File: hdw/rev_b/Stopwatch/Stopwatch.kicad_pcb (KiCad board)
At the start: 4 copper layers, 80 x 45 mm, 194 parts, among them J201 +12V IN, Q301 BSS214NW, Q302 ZXMS6004FFTA, SW601 Cap_Touch, SW602 Cap_Touch, SW603 Cap_Touch, U1001 4026, U1002 HDSP-7503, U1101 4026, U1102 HDSP-7503, U1201 4026, U1202 HDSP-7503, U1301 74LVC1G97, U1302 74LVC1G97, U1303 74LVC1G97, U1304 74LVC1G97, U1305 74LVC1G97, U1306 74LVC1G97, U1307 74LVC1G97, U1401 74LVC1G97, U1402 74LVC1G97, U1403 74LVC1G97, U1404 74LVC1G97, U1405 74LVC1G97, U1406 74LVC1G97, U1407 74LVC1G97, U201 TPS26600RHFT, U301 TPS62130A, U401 74LVC1G97, U402 CD4024, U403 CD4040, U501 74LVC1G97, U502 74LVC1G97, U503 74LVC1G97, U504 74LVC1G97, U505 74LVC1G97, U601 AT42QT1010-TSHR, U602 AT42QT1010-TSHR, U603 AT42QT1010-TSHR, U604 74LVC1G97, U605 74LVC1G97, U606 74LVC1G97, U607 74LVC1G80, U608 74LVC1G80, U701 4026, U702 HDSP-7503, U801 4026, U802 HDSP-7503, U901 4026, U902 HDSP-7503, X401 ECS-327KE

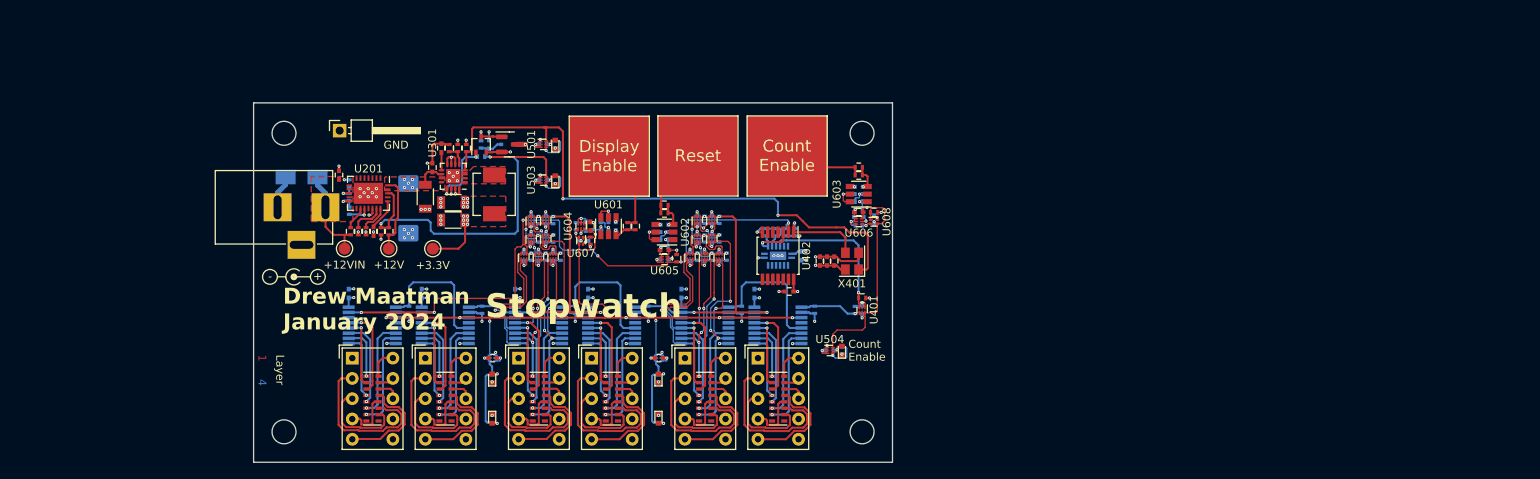
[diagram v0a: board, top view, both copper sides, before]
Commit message: converted pcb to rev b
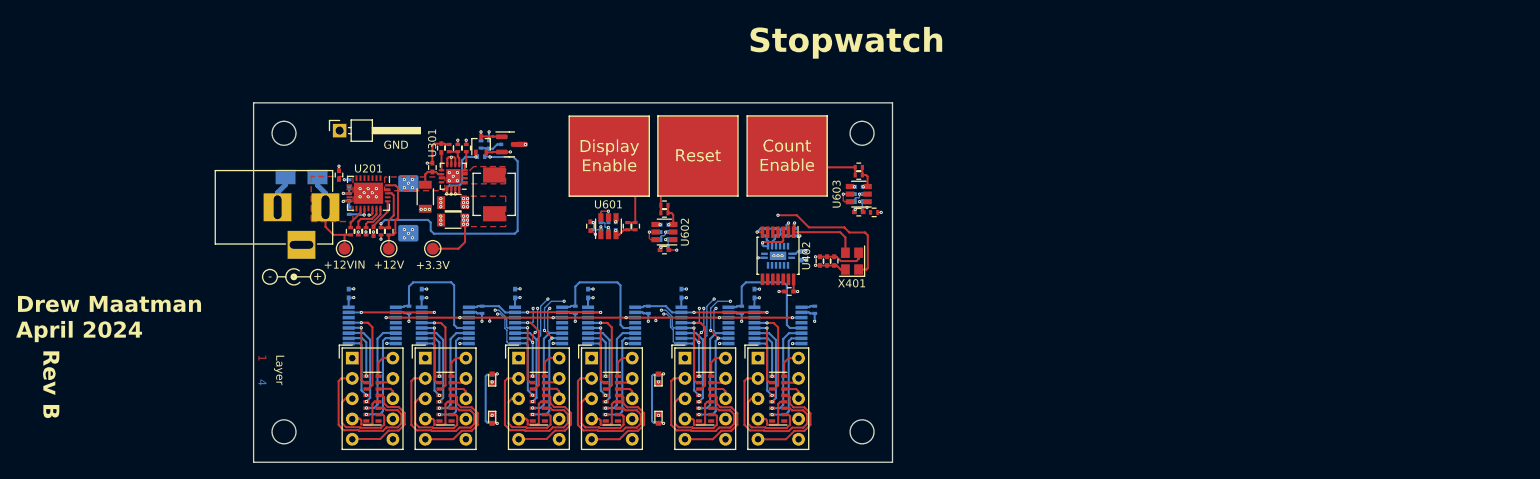
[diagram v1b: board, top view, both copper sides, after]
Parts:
- removed C1301, C1302, C1303, C1304, C1305, C1306, C1307, C1401, C1402, C1403, C1404, C1405, C1406, C1407, C405, C501, C502, C503, C504, C505, C610, C611, C612, C613, C614: 0.1uF, Capacitors_SMD:C_0402
- removed D501, D504, D505: Green, LEDs:LED_0402
- removed R1301, R1302, R1303, R1304, R1305, R1306, R1307, R1401, R1402, R1403, R1404, R1405, R1406, R1407, R402, R404, R613, R614, R615, R616: 10k, Resistors_SMD:R_0402
- removed R501, R504, R505: 1k, Resistors_SMD:R_0402
- removed U1301, U1302, U1303, U1304, U1305, U1306, U1307, U1401, U1402, U1403, U1404, U1405, U1406, U1407, U401, U501, U502, U503, U504, U505, U604, U605, U606: 74LVC1G97, Package_SON:Fairchild_MicroPak2-6_1.0x1.0mm_P0.35mm
- removed U607, U608: 74LVC1G80, Package_SON:Texas_X2SON-5_0.8x0.8mm_P0.48mm
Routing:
- net GND: track 144.6 -> 72.7 mm, vias 88 -> 61
- net Count_Reset: track 87.7 -> 17.9 mm, vias 8 -> 3
- net POS3P3_PGOOD: track 74.4 -> 20.0 mm, vias 2 -> 1
- net +3.3V: track 79.3 -> 43.8 mm, vias 62 -> 32
- net Count_Enable: track 26.2 -> 0.00 mm
- net Display_Enable: track 84.3 -> 58.6 mm
- net 1Hz_Clock_SRC: track 18.5 -> 0.00 mm, vias 1 -> 0
- net Seconds_Reset: track 32.9 -> 18.5 mm, vias 3 -> 2
- net Minutes_Reset: track 32.9 -> 18.5 mm, vias 3 -> 2
- net Stage04_SEG_B: track 23.5 -> 12.9 mm
- net Stage02_SEG_B: track 23.6 -> 13.0 mm
- net Stage04_SEG_D: track 23.4 -> 13.5 mm
- net Stage02_SEG_D: track 23.3 -> 13.5 mm
- net POS12_PGOOD: track 47.8 -> 38.5 mm
- net Stage04_SEG_G: track 29.0 -> 19.8 mm
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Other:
- board text added: "Drew Maatman April 2024"
- board text added: "Rev B"
- board text added: "Stopwatch Rev B Pads: 783 Vias: 309 Track Segments: 1922 Nets: 219 Components: 192"
- board text removed: "Drew Maatman January 2024"
- board text removed: "Stopwatch Rev A Pads: 783 Vias: 309 Track Segments: 1922 Nets: 219 Components: 192"

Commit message: integrated SC70 gates
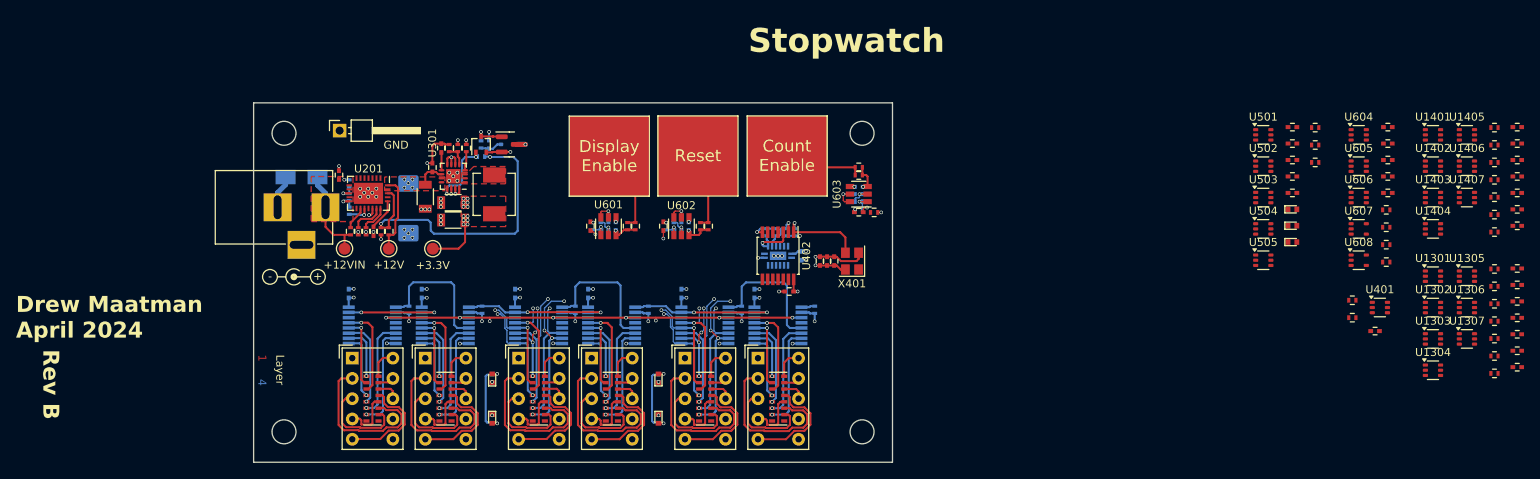
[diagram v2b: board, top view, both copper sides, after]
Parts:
- added C1301: 0.1uF, Capacitors_SMD:C_0402, F.Cu at (243.7, 102.0)
- added C1302: 0.1uF, Capacitors_SMD:C_0402, F.Cu at (243.7, 104.0)
- added C1303: 0.1uF, Capacitors_SMD:C_0402, F.Cu at (243.7, 106.1)
- added C1304: 0.1uF, Capacitors_SMD:C_0402, F.Cu at (243.7, 108.1)
- added C1305: 0.1uF, Capacitors_SMD:C_0402, F.Cu at (243.7, 110.2)
- added C1306: 0.1uF, Capacitors_SMD:C_0402, F.Cu at (243.7, 112.3)
- added C1307: 0.1uF, Capacitors_SMD:C_0402, F.Cu at (243.7, 114.3)
- added C1401: 0.1uF, Capacitors_SMD:C_0402, F.Cu at (243.7, 84.3)
- added C1402: 0.1uF, Capacitors_SMD:C_0402, F.Cu at (243.7, 86.3)
- added C1403: 0.1uF, Capacitors_SMD:C_0402, F.Cu at (243.7, 88.4)
- added C1404: 0.1uF, Capacitors_SMD:C_0402, F.Cu at (243.7, 90.4)
- added C1405: 0.1uF, Capacitors_SMD:C_0402, F.Cu at (243.7, 92.5)
- added C1406: 0.1uF, Capacitors_SMD:C_0402, F.Cu at (243.7, 94.6)
- added C1407: 0.1uF, Capacitors_SMD:C_0402, F.Cu at (243.7, 96.6)
- added C405: 0.1uF, Capacitors_SMD:C_0402, F.Cu at (225.9, 109.8)
- added C501: 0.1uF, Capacitors_SMD:C_0402, F.Cu at (215.6, 84.3)
- added C502: 0.1uF, Capacitors_SMD:C_0402, F.Cu at (215.6, 86.3)
- added C503: 0.1uF, Capacitors_SMD:C_0402, F.Cu at (215.6, 88.4)
- added C504: 0.1uF, Capacitors_SMD:C_0402, F.Cu at (215.6, 90.4)
- added C505: 0.1uF, Capacitors_SMD:C_0402, F.Cu at (215.6, 92.5)
- added C610: 0.1uF, Capacitors_SMD:C_0402, F.Cu at (227.5, 84.3)
- added C611: 0.1uF, Capacitors_SMD:C_0402, F.Cu at (227.5, 86.3)
- added C612: 0.1uF, Capacitors_SMD:C_0402, F.Cu at (227.5, 88.4)
- added C613: 0.1uF, Capacitors_SMD:C_0402, F.Cu at (227.5, 90.4)
- added C614: 0.1uF, Capacitors_SMD:C_0402, F.Cu at (227.5, 92.5)
- added D501: Green, LEDs:LED_0402, F.Cu at (215.6, 94.6)
- added D504: Green, LEDs:LED_0402, F.Cu at (215.6, 96.6)
- added D505: Green, LEDs:LED_0402, F.Cu at (215.6, 98.7)
- added R1301: 10k, Resistors_SMD:R_0402, F.Cu at (240.9, 102.0)
- added R1302: 10k, Resistors_SMD:R_0402, F.Cu at (240.9, 104.2)
- added R1303: 10k, Resistors_SMD:R_0402, F.Cu at (240.9, 106.4)
- added R1304: 10k, Resistors_SMD:R_0402, F.Cu at (240.9, 108.6)
- added R1305: 10k, Resistors_SMD:R_0402, F.Cu at (240.9, 110.7)
- added R1306: 10k, Resistors_SMD:R_0402, F.Cu at (240.9, 112.9)
- added R1307: 10k, Resistors_SMD:R_0402, F.Cu at (240.9, 115.1)
- added R1401: 10k, Resistors_SMD:R_0402, F.Cu at (240.9, 84.3)
- added R1402: 10k, Resistors_SMD:R_0402, F.Cu at (240.9, 86.5)
- added R1403: 10k, Resistors_SMD:R_0402, F.Cu at (240.9, 88.7)
- added R1404: 10k, Resistors_SMD:R_0402, F.Cu at (240.9, 90.9)
- added R1405: 10k, Resistors_SMD:R_0402, F.Cu at (240.9, 93.0)
- added R1406: 10k, Resistors_SMD:R_0402, F.Cu at (240.9, 95.2)
- added R1407: 10k, Resistors_SMD:R_0402, F.Cu at (240.9, 97.4)
- added R402: 10k, Resistors_SMD:R_0402, F.Cu at (223.1, 105.9)
- added R404: 10k, Resistors_SMD:R_0402, F.Cu at (223.1, 108.1)
- added R501: 1k, Resistors_SMD:R_0402, F.Cu at (218.4, 84.3)
- added R504: 1k, Resistors_SMD:R_0402, F.Cu at (218.4, 86.5)
- added R505: 1k, Resistors_SMD:R_0402, F.Cu at (218.4, 88.7)
- added R613: 10k, Resistors_SMD:R_0402, F.Cu at (227.3, 94.6)
- added R614: 10k, Resistors_SMD:R_0402, F.Cu at (227.3, 96.8)
- added R615: 10k, Resistors_SMD:R_0402, F.Cu at (227.3, 99.0)
- added R616: 10k, Resistors_SMD:R_0402, F.Cu at (227.3, 101.2)
- added U1301: 74LVC1G97, Package_TO_SOT_SMD:SOT-363_SC-70-6, F.Cu at (233.2, 102.9)
- added U1302: 74LVC1G97, Package_TO_SOT_SMD:SOT-363_SC-70-6, F.Cu at (233.2, 106.9)
- added U1303: 74LVC1G97, Package_TO_SOT_SMD:SOT-363_SC-70-6, F.Cu at (233.2, 110.8)
- added U1304: 74LVC1G97, Package_TO_SOT_SMD:SOT-363_SC-70-6, F.Cu at (233.2, 114.7)
- added U1305: 74LVC1G97, Package_TO_SOT_SMD:SOT-363_SC-70-6, F.Cu at (237.4, 102.9)
- added U1306: 74LVC1G97, Package_TO_SOT_SMD:SOT-363_SC-70-6, F.Cu at (237.4, 106.9)
- added U1307: 74LVC1G97, Package_TO_SOT_SMD:SOT-363_SC-70-6, F.Cu at (237.4, 110.8)
- added U1401: 74LVC1G97, Package_TO_SOT_SMD:SOT-363_SC-70-6, F.Cu at (233.2, 85.2)
- added U1402: 74LVC1G97, Package_TO_SOT_SMD:SOT-363_SC-70-6, F.Cu at (233.2, 89.2)
- added U1403: 74LVC1G97, Package_TO_SOT_SMD:SOT-363_SC-70-6, F.Cu at (233.2, 93.1)
- added U1404: 74LVC1G97, Package_TO_SOT_SMD:SOT-363_SC-70-6, F.Cu at (233.2, 97.0)
- added U1405: 74LVC1G97, Package_TO_SOT_SMD:SOT-363_SC-70-6, F.Cu at (237.4, 85.2)
- added U1406: 74LVC1G97, Package_TO_SOT_SMD:SOT-363_SC-70-6, F.Cu at (237.4, 89.2)
- added U1407: 74LVC1G97, Package_TO_SOT_SMD:SOT-363_SC-70-6, F.Cu at (237.4, 93.1)
- added U401: 74LVC1G97, Package_TO_SOT_SMD:SOT-363_SC-70-6, F.Cu at (226.5, 106.9)
- added U501: 74LVC1G97, Package_TO_SOT_SMD:SOT-363_SC-70-6, F.Cu at (211.9, 85.2)
- added U502: 74LVC1G97, Package_TO_SOT_SMD:SOT-363_SC-70-6, F.Cu at (211.9, 89.2)
- added U503: 74LVC1G97, Package_TO_SOT_SMD:SOT-363_SC-70-6, F.Cu at (211.9, 93.1)
- added U504: 74LVC1G97, Package_TO_SOT_SMD:SOT-363_SC-70-6, F.Cu at (211.9, 97.0)
- added U505: 74LVC1G97, Package_TO_SOT_SMD:SOT-363_SC-70-6, F.Cu at (211.9, 100.9)
- added U604: 74LVC1G97, Package_TO_SOT_SMD:SOT-363_SC-70-6, F.Cu at (223.9, 85.2)
- added U605: 74LVC1G97, Package_TO_SOT_SMD:SOT-363_SC-70-6, F.Cu at (223.9, 89.2)
- added U606: 74LVC1G97, Package_TO_SOT_SMD:SOT-363_SC-70-6, F.Cu at (223.9, 93.1)
- added U607: 74LVC1G80, Package_TO_SOT_SMD:SOT-353_SC-70-5, F.Cu at (223.9, 97.0)
- added U608: 74LVC1G80, Package_TO_SOT_SMD:SOT-353_SC-70-5, F.Cu at (223.9, 100.9)
- moved R604 6.07 mm to (142.4, 96.7), turned to -90 degrees
- moved R603 4.81 mm to (141.5, 96.7), turned to -90 degrees
- moved C602 3.04 mm to (140.0, 96.7), turned to -90 degrees
- moved C608 3.00 mm to (136.8, 96.7), turned to -90 degrees
- moved R611 2.65 mm to (137.2, 96.7), turned to -90 degrees
- moved C605 2.25 mm to (139.1, 96.7), turned to -90 degrees
- moved U602 2.25 mm to (139.1, 96.7), turned to 90 degrees
- moved R608 2.05 mm to (138.1, 96.7), turned to 90 degrees
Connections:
- U403 pad 17: GND -> (no net)
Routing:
- net POS3P3_PGOOD: track 20.0 -> 2.39 mm, vias 1 -> 0
- net Net-(SW602-TP): track 9.06 -> 9.84 mm
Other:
- board text added: "Stopwatch Rev B Pads: Vias: Track Segments: Nets: Components:"
- board text removed: "Stopwatch Rev B Pads: 783 Vias: 309 Track Segments: 1922 Nets: 219 Components: 192"

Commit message: some rev B PCB progress
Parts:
- C405, C501, C503, C504, C610, C611, C612, C613, C614, R404, R501, R504, R505, R613, R614, R615, R616, R617, U502, U505: moved to B.Cu
- moved C613 104.8 mm to (122.9, 96.7), turned to -90 degrees
- moved R616 103.5 mm to (123.9, 96.7), turned to -90 degrees
- moved C610 102.5 mm to (125.8, 96.7), turned to 90 degrees
- moved R614 102.5 mm to (124.9, 96.7), turned to 90 degrees
- moved C505 102.3 mm to (115.4, 112.9)
- moved U607 100.9 mm to (122.9, 96.7), turned to 90 degrees
- moved U604 98.7 mm to (125.8, 96.7), turned to -90 degrees
- moved U505 97.3 mm to (115.4, 112.9), turned to 180 degrees
- moved R501 94.8 mm to (123.8, 90.1), turned to -90 degrees
- moved R504 94.6 mm to (123.8, 87.2), turned to -90 degrees
- moved C501 94.2 mm to (121.6, 90.1), turned to 180 degrees
- moved C503 94.0 mm to (121.6, 87.2), turned to 180 degrees
- moved D504 92.2 mm to (123.8, 87.2), turned to -90 degrees
- moved R613 92.1 mm to (135.3, 96.7), turned to 90 degrees
- moved C611 91.9 mm to (136.2, 96.7), turned to 90 degrees
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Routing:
- net 32768Hz_Clock: track 10.6 -> 4.79 mm
- net GND: track 72.7 -> 71.3 mm, vias 61 -> 59
- net Net-(SW602-TP): track 9.84 -> 10.4 mm

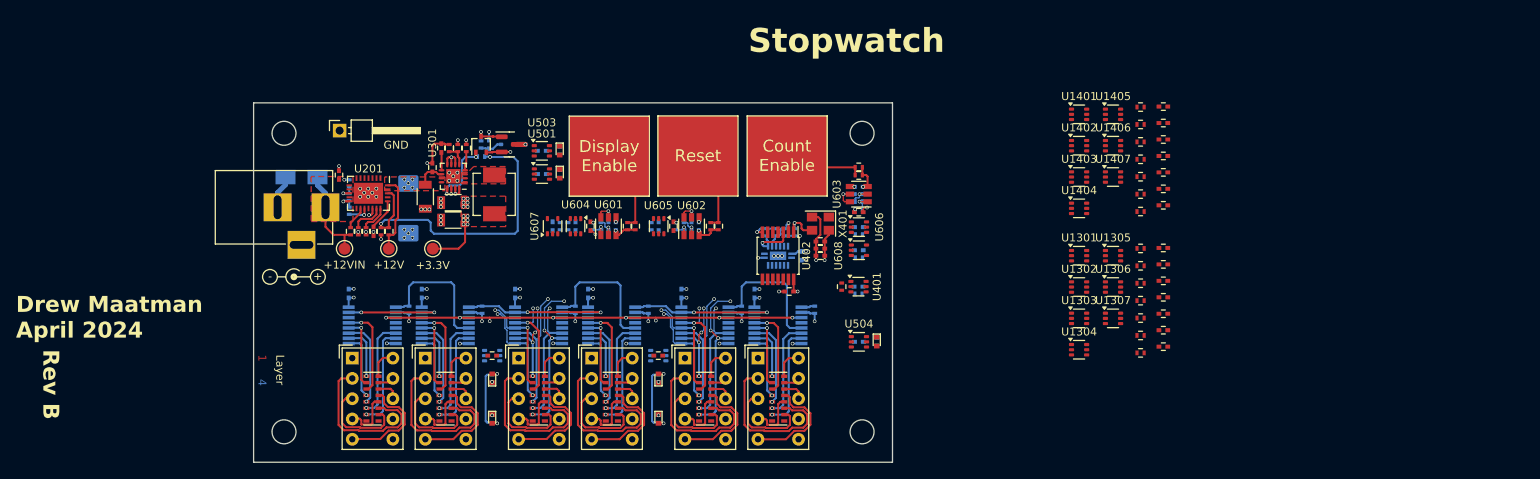
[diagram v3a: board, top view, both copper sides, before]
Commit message: moved all components into rev b board outline
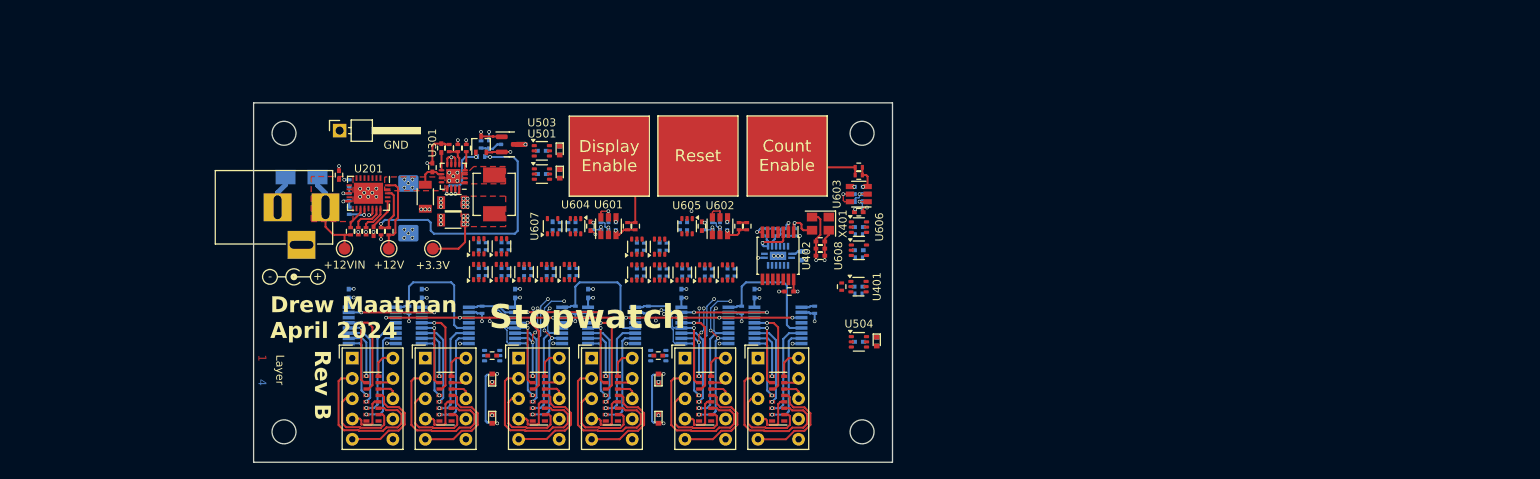
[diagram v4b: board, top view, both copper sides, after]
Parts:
- C1301, C1302, C1303, C1304, C1305, C1306, C1307, C1401, C1402, C1403, C1404, C1405, C1406, C1407, R1301, R1302, R1303, R1304, R1305, R1306, R1307, R1401, R1402, R1403, R1404, R1405, R1406, R1407: moved to B.Cu
- moved C1401 88.2 mm to (113.7, 102.4), turned to -90 degrees
- moved C1406 86.0 mm to (113.7, 99.2), turned to -90 degrees
- moved C1402 84.9 mm to (116.5, 102.4), turned to -90 degrees
- moved R1401 84.5 mm to (114.6, 102.4), turned to -90 degrees
- moved C1407 83.0 mm to (116.5, 99.2), turned to -90 degrees
- moved R1406 82.2 mm to (114.6, 99.2), turned to -90 degrees
- moved C1403 81.7 mm to (119.4, 102.4), turned to -90 degrees
- moved R1402 81.2 mm to (117.5, 102.4), turned to -90 degrees
- moved U1406 80.4 mm to (113.7, 99.2), turned to 90 degrees
- moved R1407 79.2 mm to (117.5, 99.2), turned to -90 degrees
- moved C1404 78.6 mm to (122.2, 102.4), turned to -90 degrees
- moved R1403 78.0 mm to (120.3, 102.4), turned to -90 degrees
- moved U1401 77.7 mm to (113.7, 102.4), turned to 90 degrees
- moved U1407 77.1 mm to (116.5, 99.2), turned to 90 degrees
- moved C1405 75.4 mm to (125.0, 102.4), turned to -90 degrees
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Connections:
- R1401 pad 1: Net-(R1401-Pad1) -> Net-(R1301-Pad1)
- R1402 pad 1: Net-(R1402-Pad1) -> Net-(R1302-Pad1)
- R1403 pad 1: Net-(R1403-Pad1) -> Net-(R1303-Pad1)
- R1404 pad 1: Net-(R1404-Pad1) -> Net-(R1304-Pad1)
- R1405 pad 1: Net-(R1405-Pad1) -> Net-(R1305-Pad1)
- R1406 pad 1: Net-(R1406-Pad1) -> Net-(R1306-Pad1)
- R1407 pad 1: Minutes_Reset -> Seconds_Reset
- U1401 pad 1: Stage04_SEG_D -> Stage02_SEG_D
- U1401 pad 4: Net-(R1401-Pad1) -> Net-(R1301-Pad1)
- U1401 pad 6: Stage04_SEG_B -> Stage02_SEG_B
- U1402 pad 3: Stage04_SEG_A -> Stage02_SEG_A
- U1402 pad 4: Net-(R1402-Pad1) -> Net-(R1302-Pad1)
- U1402 pad 6: Stage04_SEG_C -> Stage02_SEG_C
- U1403 pad 3: Stage04_SEG_F -> Stage02_SEG_F
- U1403 pad 4: Net-(R1403-Pad1) -> Net-(R1303-Pad1)
- U1403 pad 6: Stage04_SEG_E -> Stage02_SEG_E
- U1404 pad 3: Net-(R1402-Pad1) -> Net-(R1302-Pad1)
- U1404 pad 4: Net-(R1404-Pad1) -> Net-(R1304-Pad1)
- U1404 pad 6: Net-(R1401-Pad1) -> Net-(R1301-Pad1)
- U1405 pad 3: Stage04_SEG_G -> Stage02_SEG_G
- U1405 pad 4: Net-(R1405-Pad1) -> Net-(R1305-Pad1)
- U1405 pad 6: Net-(R1403-Pad1) -> Net-(R1303-Pad1)
- U1406 pad 3: Net-(R1405-Pad1) -> Net-(R1305-Pad1)
- U1406 pad 4: Net-(R1406-Pad1) -> Net-(R1306-Pad1)
- U1406 pad 6: Net-(R1404-Pad1) -> Net-(R1304-Pad1)
- U1407 pad 4: Minutes_Reset -> Seconds_Reset
- U1407 pad 6: Net-(R1406-Pad1) -> Net-(R1306-Pad1)
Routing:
- net Net-(SW602-TP): track 10.4 -> 4.58 mm

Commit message: more PCB work
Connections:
- R1401 pad 1: Net-(R1301-Pad1) -> Net-(R1401-Pad1)
- R1402 pad 1: Net-(R1302-Pad1) -> Net-(R1402-Pad1)
- R1403 pad 1: Net-(R1303-Pad1) -> Net-(R1403-Pad1)
- R1404 pad 1: Net-(R1304-Pad1) -> Net-(R1404-Pad1)
- R1405 pad 1: Net-(R1305-Pad1) -> Net-(R1405-Pad1)
- R1406 pad 1: Net-(R1306-Pad1) -> Net-(R1406-Pad1)
- R1407 pad 1: Seconds_Reset -> Minutes_Reset
- U1401 pad 1: Stage02_SEG_D -> Stage04_SEG_D
- U1401 pad 4: Net-(R1301-Pad1) -> Net-(R1401-Pad1)
- U1401 pad 6: Stage02_SEG_B -> Stage04_SEG_B
- U1402 pad 3: Stage02_SEG_A -> Stage04_SEG_A
- U1402 pad 4: Net-(R1302-Pad1) -> Net-(R1402-Pad1)
- U1402 pad 6: Stage02_SEG_C -> Stage04_SEG_C
- U1403 pad 3: Stage02_SEG_F -> Stage04_SEG_F
- U1403 pad 4: Net-(R1303-Pad1) -> Net-(R1403-Pad1)
- U1403 pad 6: Stage02_SEG_E -> Stage04_SEG_E
- U1404 pad 3: Net-(R1302-Pad1) -> Net-(R1402-Pad1)
- U1404 pad 4: Net-(R1304-Pad1) -> Net-(R1404-Pad1)
- U1404 pad 6: Net-(R1301-Pad1) -> Net-(R1401-Pad1)
- U1405 pad 3: Stage02_SEG_G -> Stage04_SEG_G
- U1405 pad 4: Net-(R1305-Pad1) -> Net-(R1405-Pad1)
- U1405 pad 6: Net-(R1303-Pad1) -> Net-(R1403-Pad1)
- U1406 pad 3: Net-(R1305-Pad1) -> Net-(R1405-Pad1)
- U1406 pad 4: Net-(R1306-Pad1) -> Net-(R1406-Pad1)
- U1406 pad 6: Net-(R1304-Pad1) -> Net-(R1404-Pad1)
- U1407 pad 4: Seconds_Reset -> Minutes_Reset
- U1407 pad 6: Net-(R1306-Pad1) -> Net-(R1406-Pad1)
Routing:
- net GND: track 71.3 -> 152.4 mm, vias 59 -> 82
- net Count_Reset: track 17.9 -> 85.6 mm, vias 3 -> 7
- net +3.3V: track 43.8 -> 96.8 mm, vias 32 -> 57
- net POS3P3_PGOOD: track 2.39 -> 54.5 mm, vias 0 -> 2
- net Display_Enable: track 58.6 -> 87.1 mm, vias 8 -> 9
- net Net-(R1404-Pad1): track 0.00 -> 16.4 mm, vias 0 -> 2
- net Net-(R1304-Pad1): track 0.00 -> 15.8 mm, vias 0 -> 2
- net 1Hz_Clock_SRC: track 0.00 -> 15.6 mm, vias 0 -> 1
- net Count_Enable: track 0.00 -> 14.9 mm, vias 0 -> 1
- net Net-(R1405-Pad1): track 0.00 -> 14.5 mm, vias 0 -> 3
- net Net-(R1305-Pad1): track 0.00 -> 14.2 mm, vias 0 -> 3
- net Seconds_Reset: track 18.5 -> 32.5 mm, vias 2 -> 3
- net Minutes_Reset: track 18.5 -> 31.5 mm, vias 2 -> 4
- net Stage02_SEG_C: track 13.8 -> 23.9 mm
- net Stage04_SEG_C: track 13.6 -> 23.3 mm
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
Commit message: finished rev B PCB
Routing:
- net Stage02_SEG_A: track 17.9 -> 19.0 mm
- net Net-(U201-RTN): track 3.98 -> 3.04 mm
- net Stage02_SEG_B: track 22.6 -> 21.9 mm
- net GND: track 152.4 -> 151.8 mm, vias 82 -> 81
- net +3.3V: track 96.8 -> 97.4 mm
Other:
- board text added: "Stopwatch Rev B Pads: 775 Vias: 303 Track Segments: 1818 Nets: 219 Components: 182"
- board text removed: "Stopwatch Rev B Pads: Vias: Track Segments: Nets: Components:"
